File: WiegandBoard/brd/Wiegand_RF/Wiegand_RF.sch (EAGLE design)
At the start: 58 parts, among them IC9 LM1117, Q1 NTR1P02T1G, Q2 NTR1P02T1G

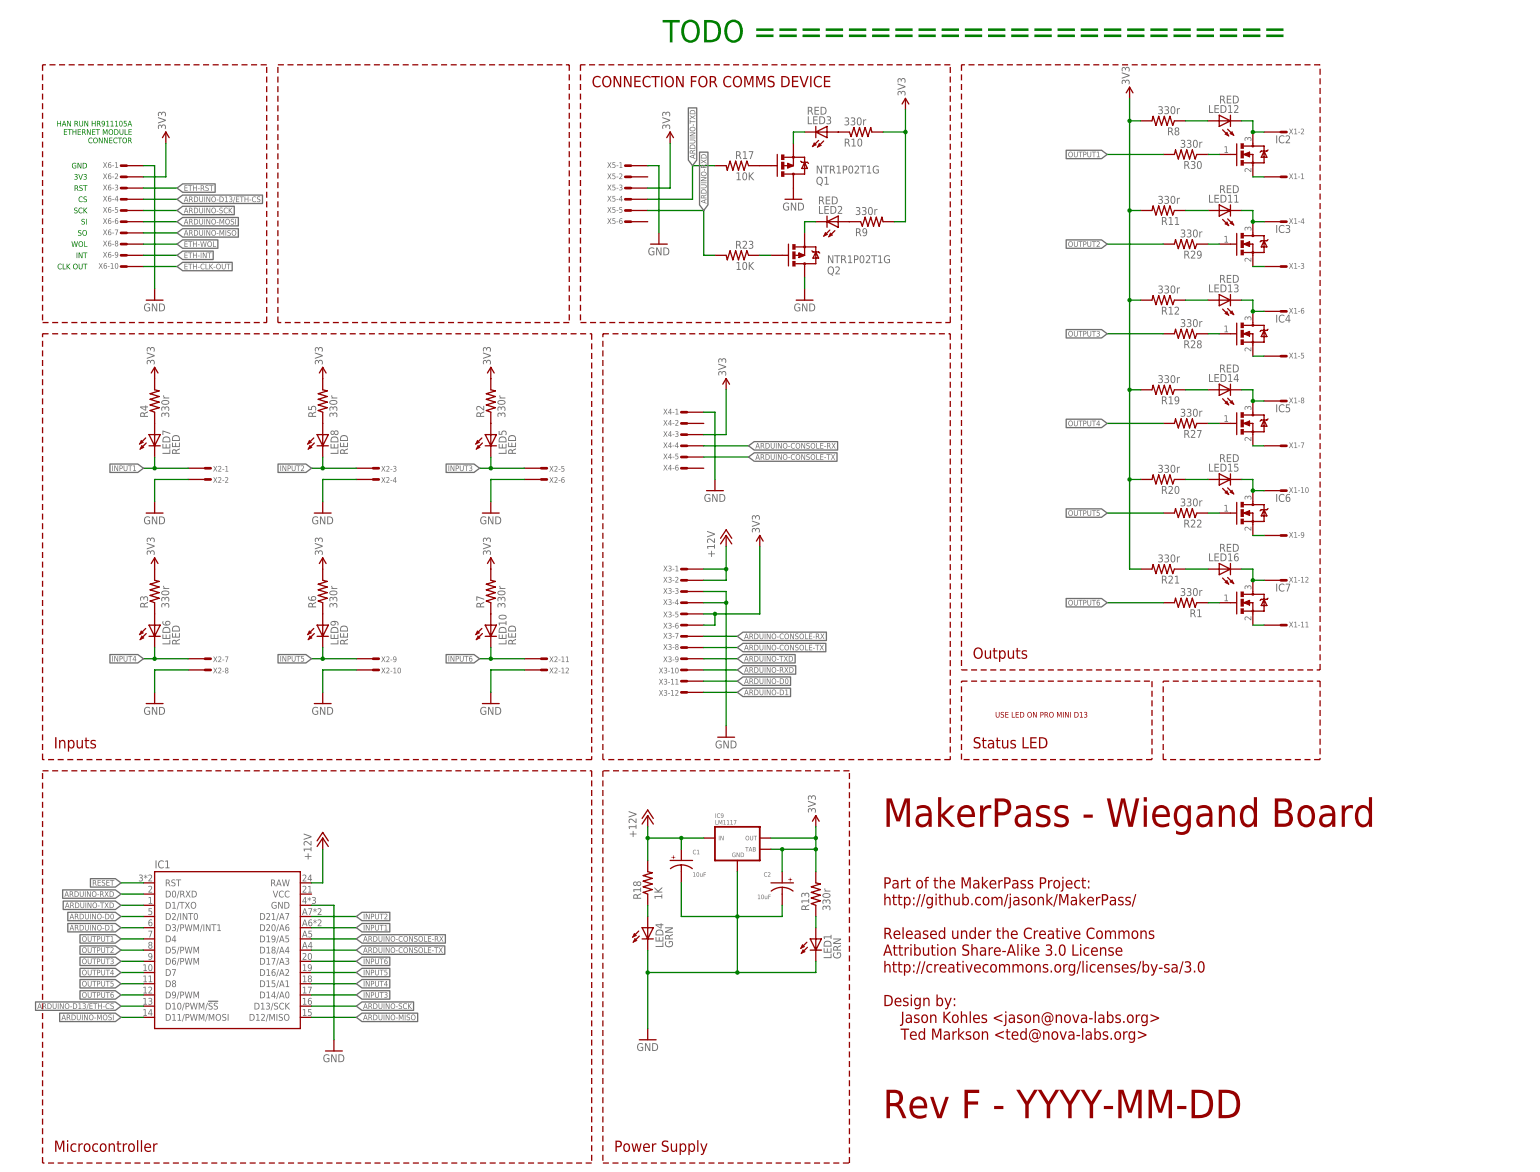
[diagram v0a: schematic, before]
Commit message: cleaned rs485 files, updated RF version for production - REV F
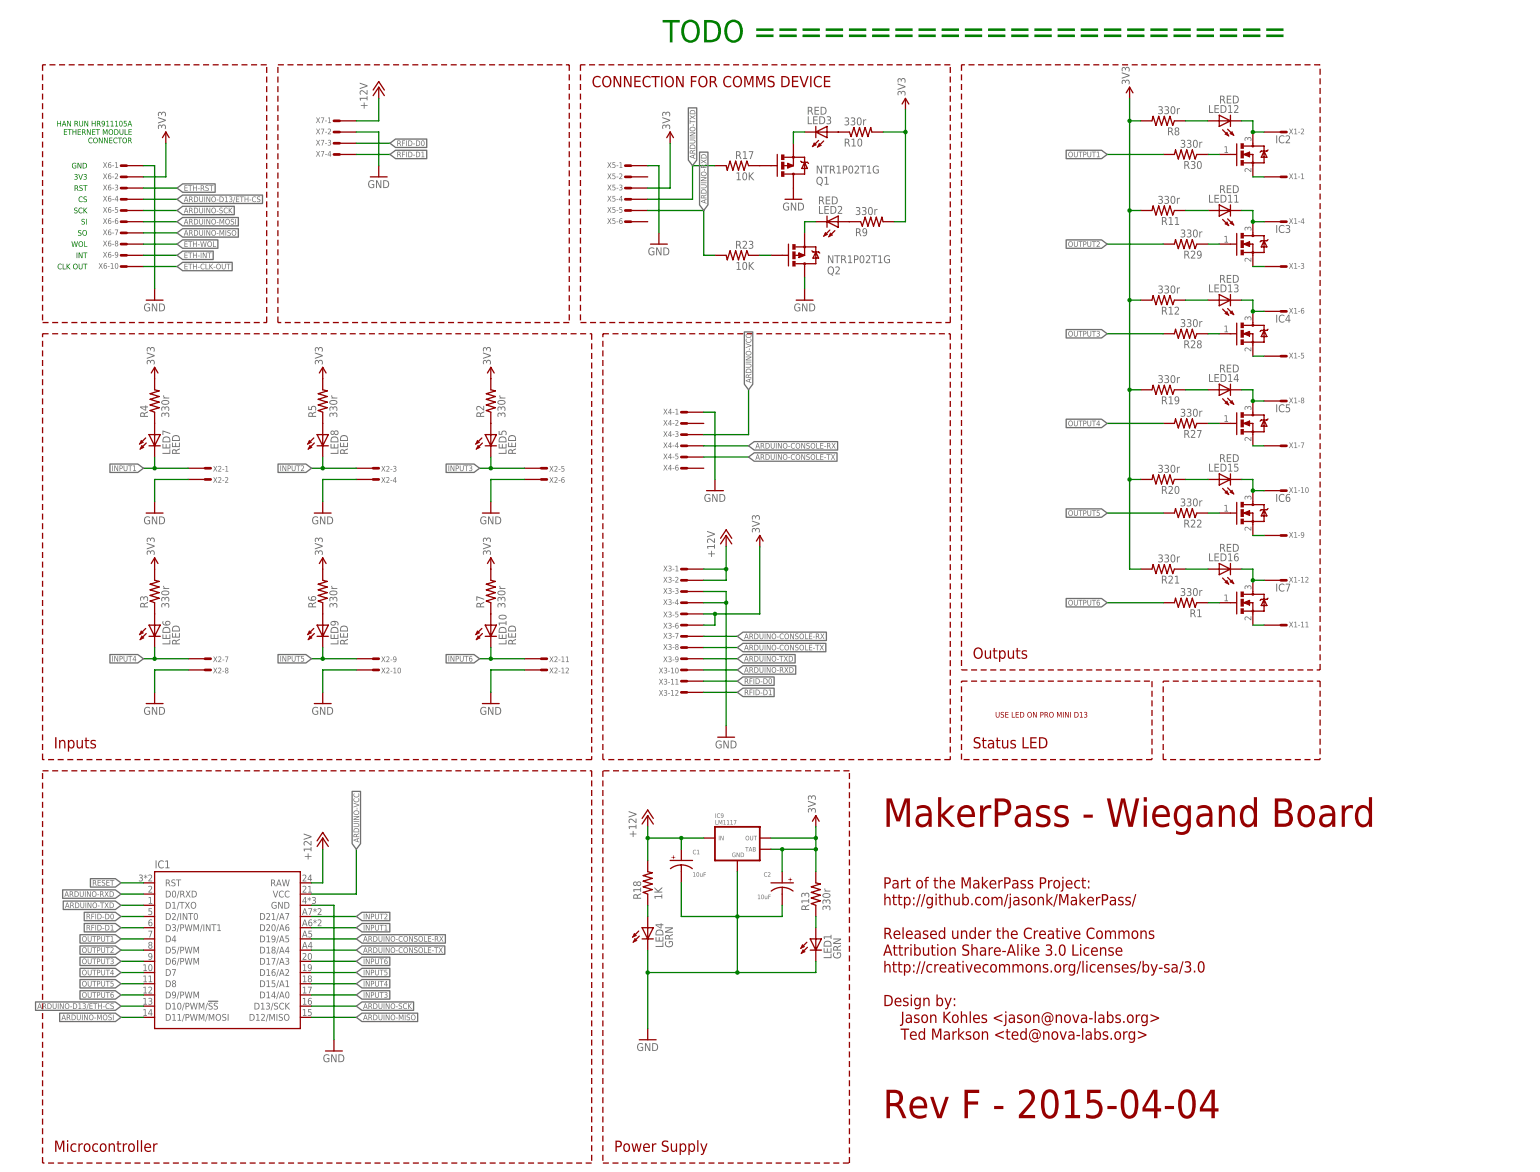
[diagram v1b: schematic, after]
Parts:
- added X7: (no value), Lumisense:CON-1X4
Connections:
- removed net ARDUINO-D0: IC1.D2/INT0, X3-11.S
- removed net ARDUINO-D1: IC1.D3/PWM/INT1, X3-12.S
- new net ARDUINO-VCC: IC1.VCC, X4-3.S
- new net RFID-D0: IC1.D2/INT0, X3-11.S, X7-3.S
- new net RFID-D1: IC1.D3/PWM/INT1, X3-12.S, X7-4.S
- net +12V: now also X7-1.S
- net 3V3: no longer X4-3.S
- net GND: now also X7-2.S
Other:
- note added: "Rev F - 2015-04-04"
- note removed: "Rev F - YYYY-MM-DD"
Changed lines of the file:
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@@
 <part name="U$4" library="Lumisense" deviceset="3V3" device=""/>
 <part name="U$5" library="Lumisense" deviceset="3V3" device=""/>
-<part name="U$6" library="Lumisense" deviceset="3V3" device=""/>
 <part name="U$7" library="Lumisense" deviceset="3V3" device=""/>
 <part name="U$8" library="Lumisense" deviceset="3V3" device=""/>
@@
 <part name="U$15" library="Lumisense" deviceset="3V3" device=""/>
 <part name="GND9" library="SparkFun" deviceset="GND" device=""/>
+<part name="X7" library="Lumisense" deviceset="CON-1X4" device=""/>
+<part name="P+1" library="supply1" deviceset="+12V" device=""/>
+<part name="GND10" library="SparkFun" deviceset="GND" device=""/>
 </parts>
 <sheets>
@@
 <text x="7.62" y="10.16" size="2.54" layer="94">Microcontroller</text>
 <text x="195.58" y="83.82" size="6.4516" layer="94">MakerPass - Wiegand Board</text>
-<text x="195.58" y="17.78" size="6.4516" layer="94">Rev F - YYYY-MM-DD</text>
+<text x="195.58" y="17.78" size="6.4516" layer="94">Rev F - 2015-04-04</text>
 <text x="287.02" y="261.62" size="5.08" layer="91" align="bottom-right">TODO =======================
 </text>
@@
 <instance part="U$4" gate="G$1" x="200.66" y="246.38"/>
 <instance part="U$5" gate="G$1" x="251.46" y="248.92"/>
-<instance part="U$6" gate="G$1" x="160.02" y="182.88"/>
 <instance part="U$7" gate="G$1" x="167.64" y="147.32"/>
 <instance part="U$8" gate="G$1" x="106.68" y="142.24"/>
@@
 <instance part="U$15" gate="G$1" x="33.02" y="238.76"/>
 <instance part="GND9" gate="1" x="30.48" y="203.2"/>
+<instance part="X7" gate="-1" x="71.12" y="243.84"/>
+<instance part="X7" gate="-2" x="71.12" y="241.3"/>
+<instance part="X7" gate="-3" x="71.12" y="238.76"/>
+<instance part="X7" gate="-4" x="71.12" y="236.22"/>
+<instance part="P+1" gate="1" x="81.28" y="251.46"/>
+<instance part="GND10" gate="1" x="81.28" y="231.14"/>
 </instances>
 <busses>
@@
 <pinref part="GND9" gate="1" pin="GND"/>
 </segment>
+<segment>
+<pinref part="X7" gate="-2" pin="S"/>
+<pinref part="GND10" gate="1" pin="GND"/>
+<wire x1="76.2" y1="241.3" x2="81.28" y2="241.3" width="0.1524" layer="91"/>
+<wire x1="81.28" y1="241.3" x2="81.28" y2="233.68" width="0.1524" layer="91"/>
+</segment>
 </net>
 <net name="ARDUINO-MISO" class="0">
@@
 <junction x="160.02" y="142.24"/>
 </segment>
+<segment>
+<pinref part="X7" gate="-1" pin="S"/>
+<pinref part="P+1" gate="1" pin="+12V"/>
+<wire x1="76.2" y1="243.84" x2="81.28" y2="243.84" width="0.1524" layer="91"/>
+<wire x1="81.28" y1="243.84" x2="81.28" y2="248.92" width="0.1524" layer="91"/>
+</segment>
 </net>
 <net name="N$8" class="0">
@@
 </segment>
 </net>
-<net name="ARDUINO-D1" class="0">
+<net name="RFID-D1" class="0">
 <segment>
 <pinref part="IC1" gate="G$1" pin="D3/PWM/INT1"/>
@@
 <label x="162.56" y="114.3" size="1.27" layer="95" xref="yes"/>
 </segment>
-</net>
-<net name="ARDUINO-D0" class="0">
+<segment>
+<pinref part="X7" gate="-4" pin="S"/>
+<wire x1="76.2" y1="236.22" x2="83.82" y2="236.22" width="0.1524" layer="91"/>
+<label x="83.82" y="236.22" size="1.27" layer="95" xref="yes"/>
+</segment>
+</net>
+<net name="RFID-D0" class="0">
 <segment>
 <pinref part="IC1" gate="G$1" pin="D2/INT0"/>
@@
 <wire x1="154.94" y1="116.84" x2="162.56" y2="116.84" width="0.1524" layer="91"/>
 <label x="162.56" y="116.84" size="1.27" layer="95" xref="yes"/>
+</segment>
+<segment>
+<label x="83.82" y="238.76" size="1.27" layer="95" xref="yes"/>
+<pinref part="X7" gate="-3" pin="S"/>
+<wire x1="76.2" y1="238.76" x2="83.82" y2="238.76" width="0.1524" layer="91"/>
 </segment>
 </net>
@@
 </segment>
 <segment>
-<pinref part="X4" gate="-3" pin="S"/>
-<wire x1="154.94" y1="172.72" x2="160.02" y2="172.72" width="0.1524" layer="91"/>
-<wire x1="160.02" y1="172.72" x2="160.02" y2="182.88" width="0.1524" layer="91"/>
-<pinref part="U$6" gate="G$1" pin="3V3"/>
-</segment>
-<segment>
 <pinref part="R7" gate="G$1" pin="2"/>
 <pinref part="U$8" gate="G$1" pin="3V3"/>
@@
 </segment>
 </net>
+<net name="ARDUINO-VCC" class="0">
+<segment>
+<pinref part="X4" gate="-3" pin="S"/>
+<label x="165.1" y="182.88" size="1.27" layer="95" rot="R90" xref="yes"/>
+<wire x1="154.94" y1="172.72" x2="165.1" y2="172.72" width="0.1524" layer="91"/>
+<wire x1="165.1" y1="172.72" x2="165.1" y2="182.88" width="0.1524" layer="91"/>
+</segment>
+<segment>
+<pinref part="IC1" gate="G$1" pin="VCC"/>
+<wire x1="66.04" y1="68.58" x2="76.2" y2="68.58" width="0.1524" layer="91"/>
+<wire x1="76.2" y1="68.58" x2="76.2" y2="78.74" width="0.1524" layer="91"/>
+<label x="76.2" y="78.74" size="1.27" layer="95" rot="R90" xref="yes"/>
+</segment>
+</net>
